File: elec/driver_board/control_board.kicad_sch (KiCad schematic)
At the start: 11 parts, among them J47 button_shutdown, J48 button_mode, J49 rotary_encoder, J50 DCF77 board, J51 RTC, U1 ESP32-C3-DEVKITM-1

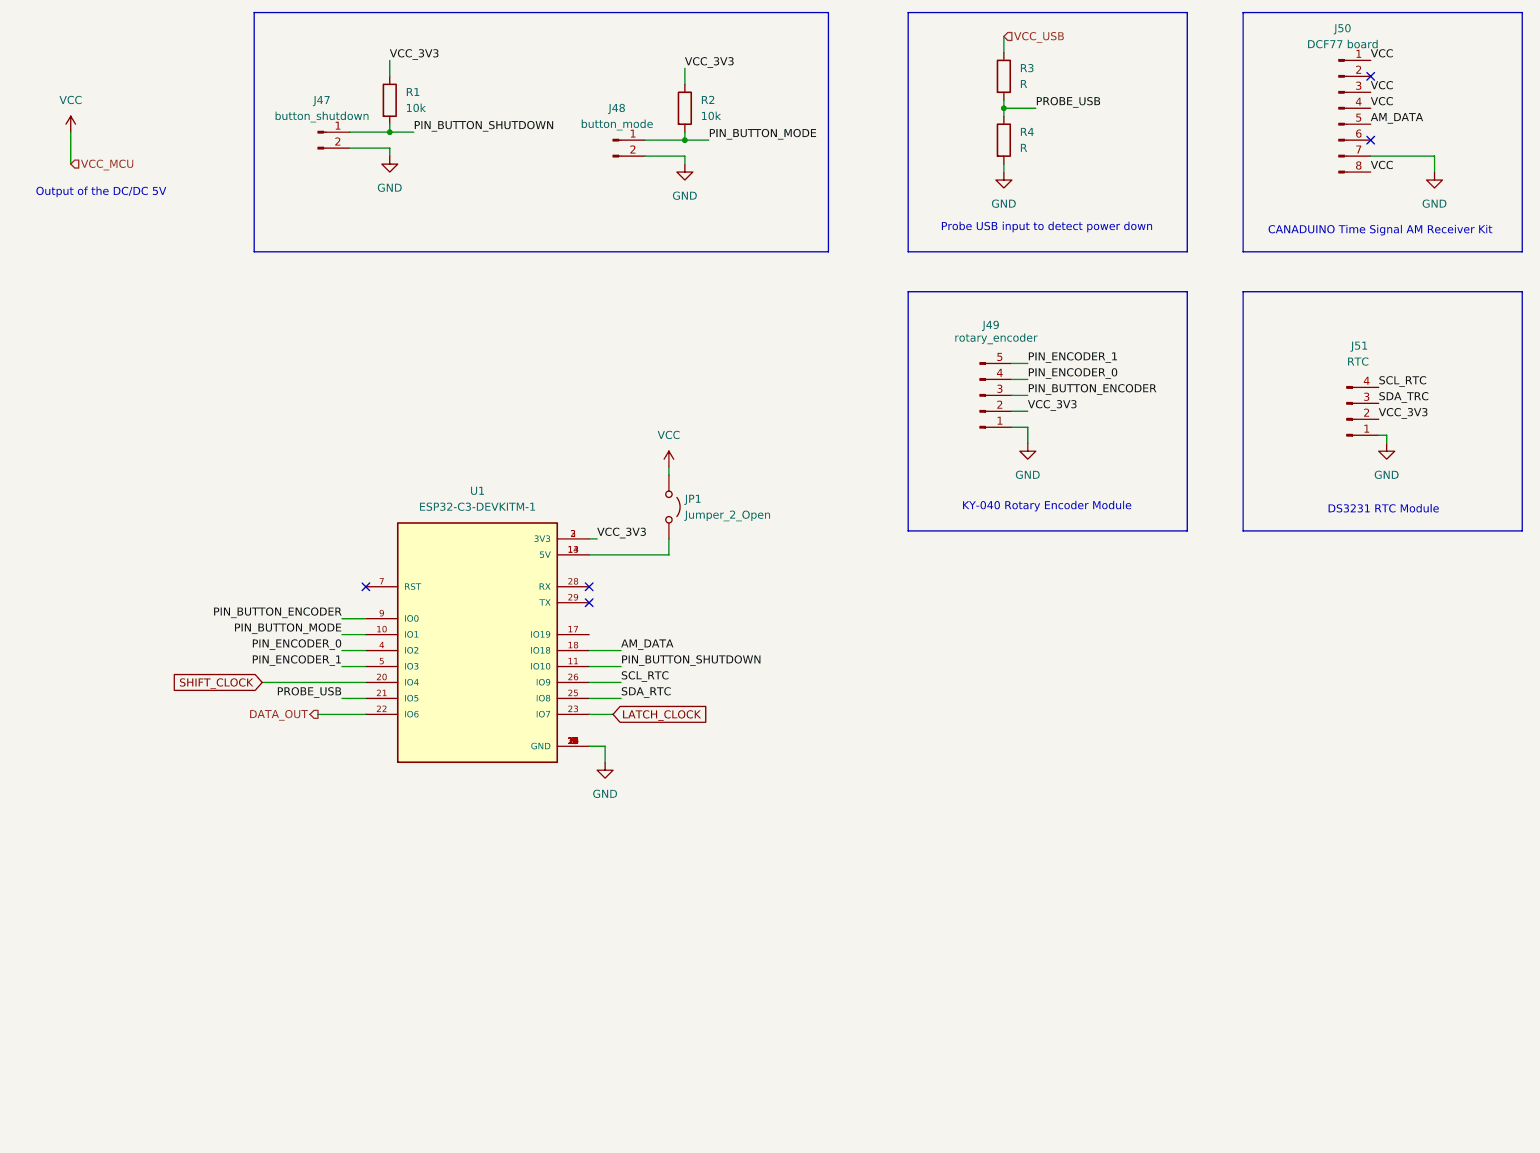
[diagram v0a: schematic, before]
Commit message: [elec] New design with BKA30D-R5
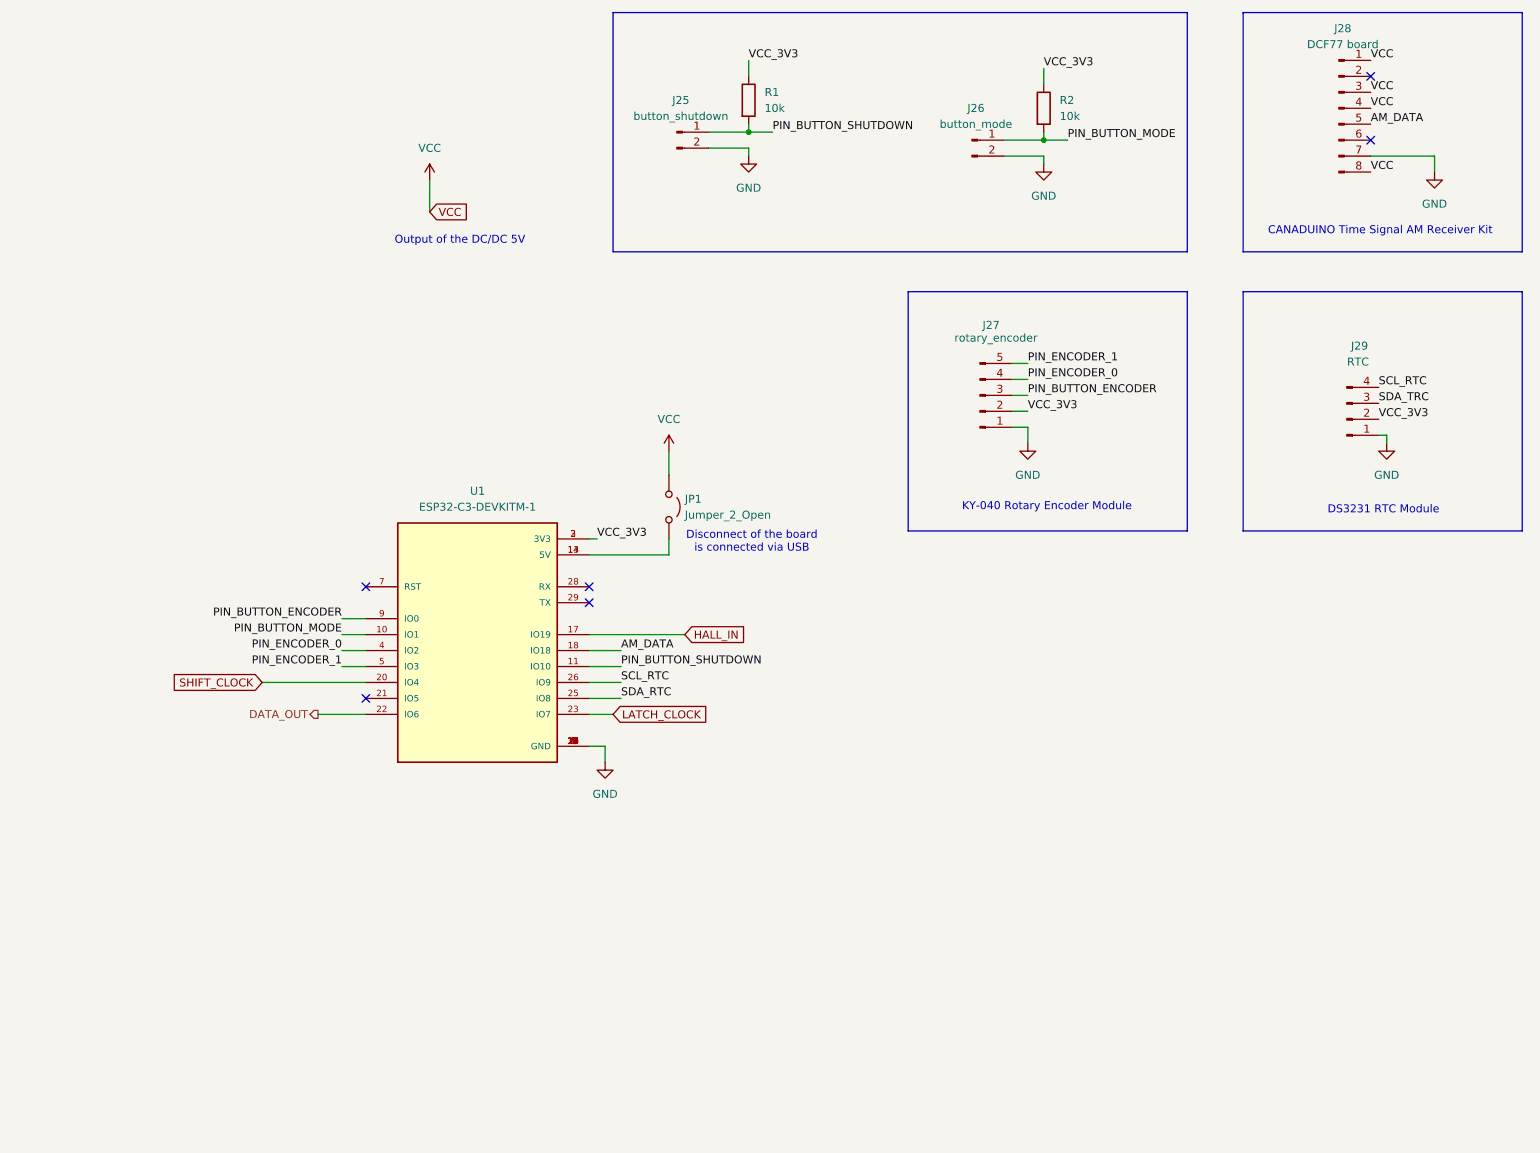
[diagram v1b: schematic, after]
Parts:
- removed R3, R4: R, Resistor_SMD:R_0805_2012Metric, symbol Device:R
- renumbered J47 to J25, J48 to J26, J49 to J27, J50 to J28, J51 to J29
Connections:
- net HALL_IN: now reaches U1.17 (IO19)
- net PROBE_USB: no longer names the net of U1.21 (IO5)
- no-connect marks 5 -> 6
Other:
- note added: "Disconnect of the board is connected via USB"
- note removed: "Probe USB input to detect power down"
- moved on the sheet: J25, J26, R1, R2

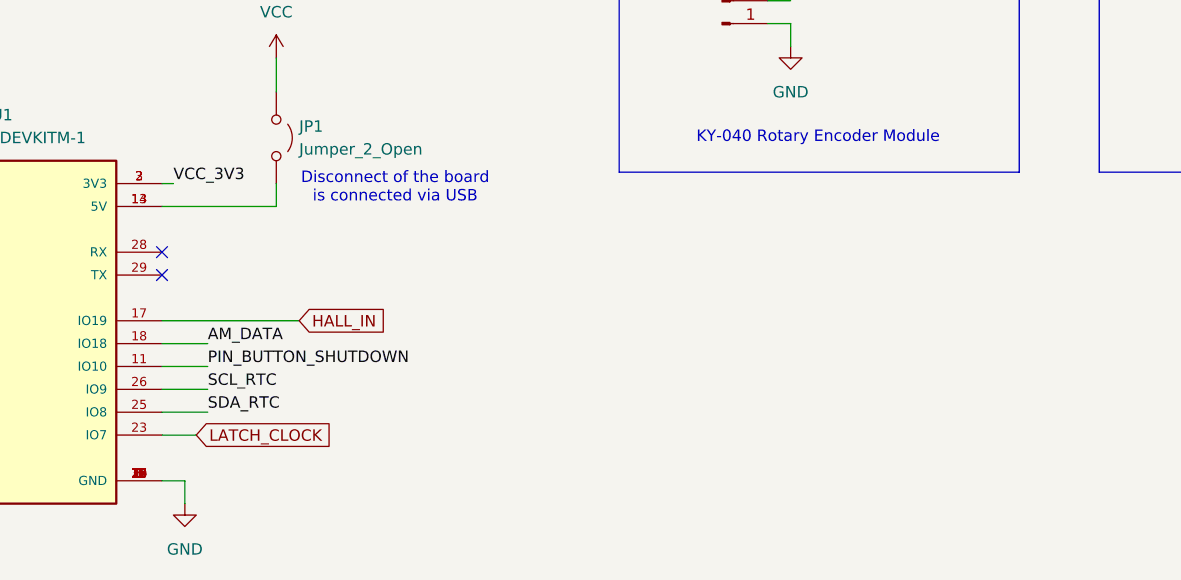
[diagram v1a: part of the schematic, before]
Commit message: [elec] continue routing
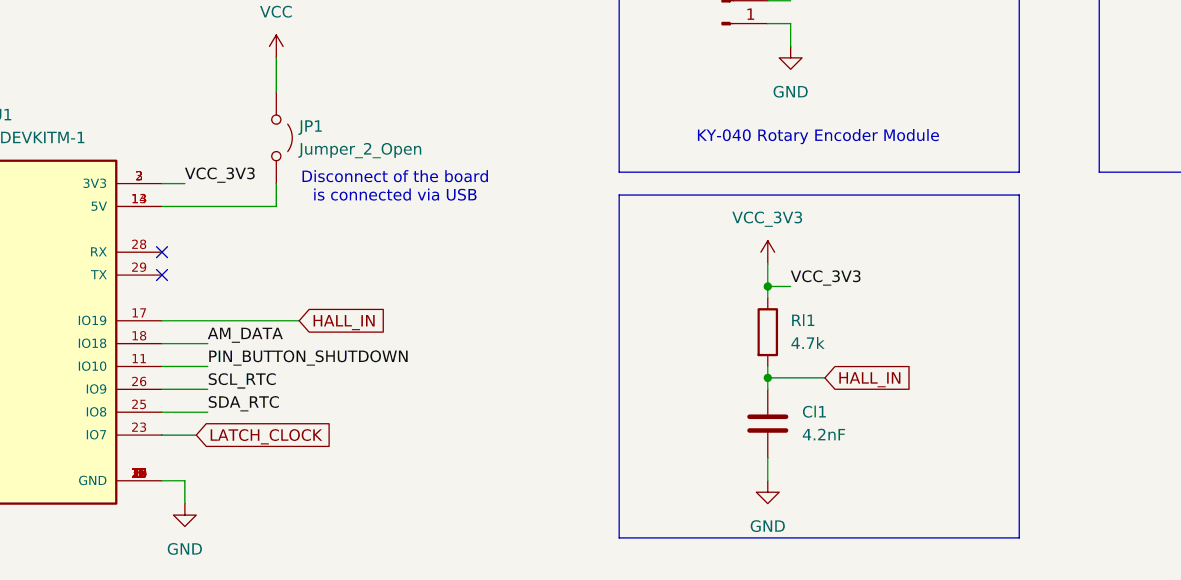
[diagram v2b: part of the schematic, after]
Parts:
- added Cl1: 4.2nF, Capacitor_SMD:C_1206_3216Metric, symbol Device:C
- added Rl1: 4.7k, Capacitor_SMD:C_1206_3216Metric, symbol Device:R
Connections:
- net GND: now also Cl1.2
- net HALL_IN: now also Cl1.1, Rl1.2
- net VCC_3V3: now also Rl1.1

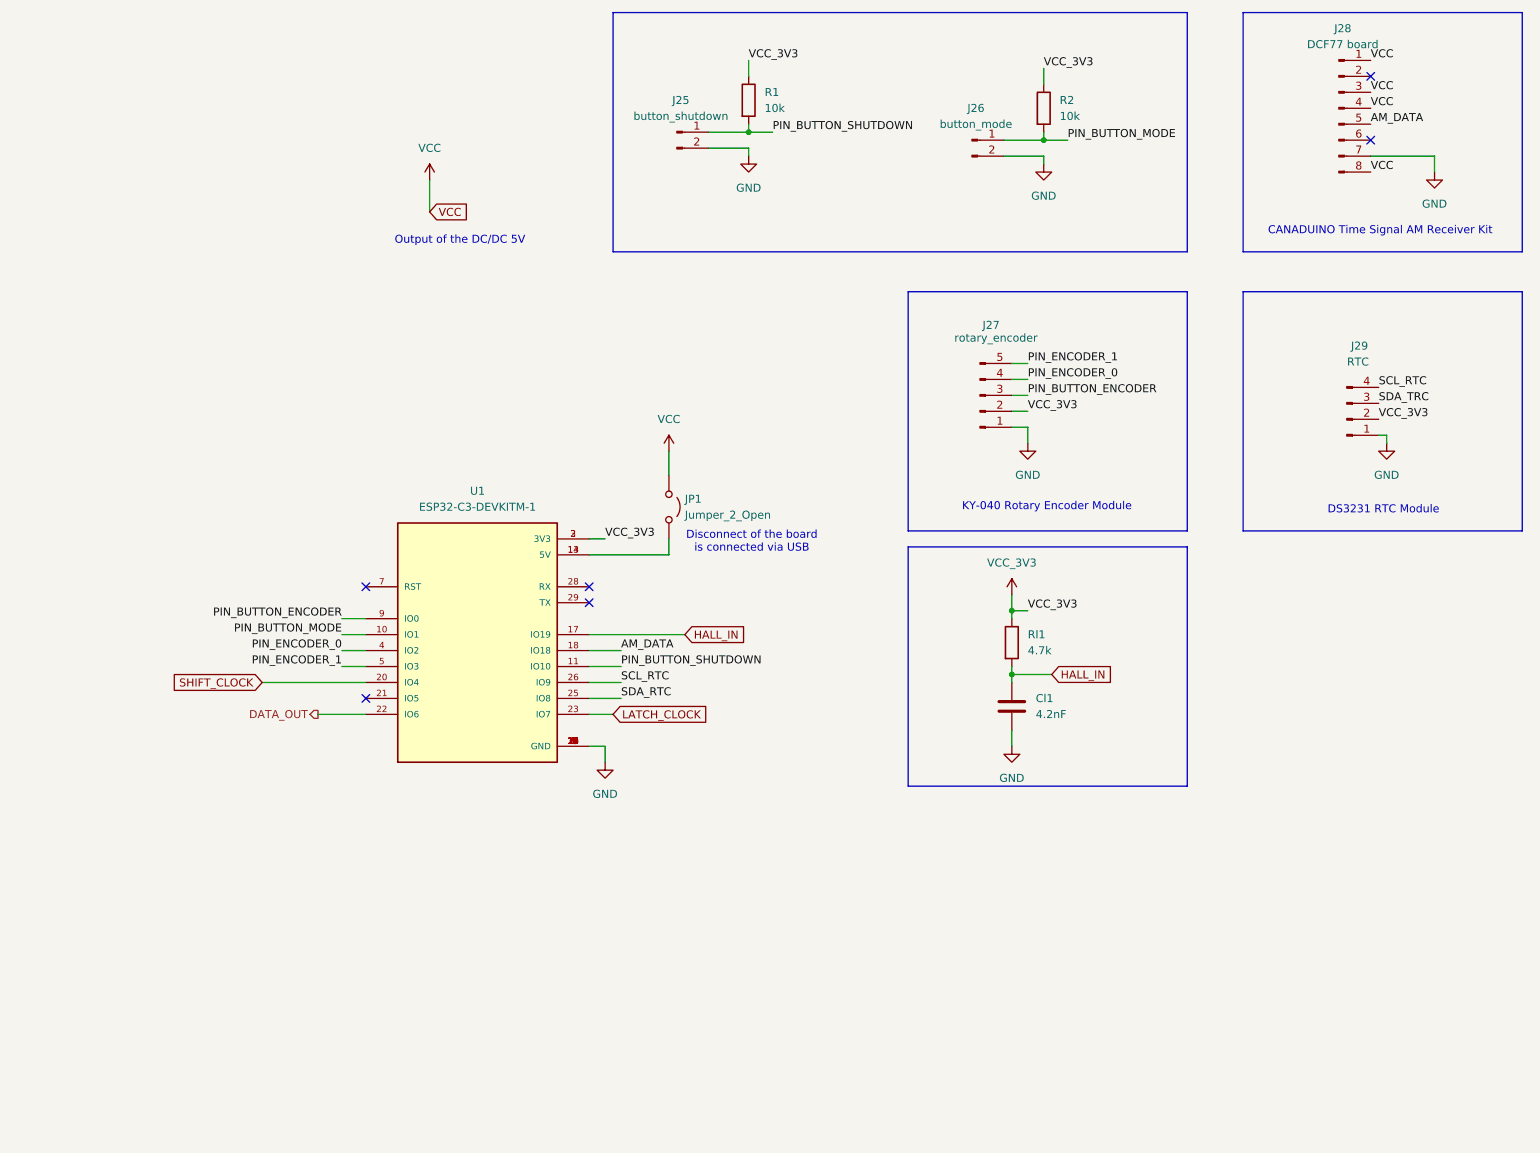
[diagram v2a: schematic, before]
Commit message: [elec] First version of the routing of driver board
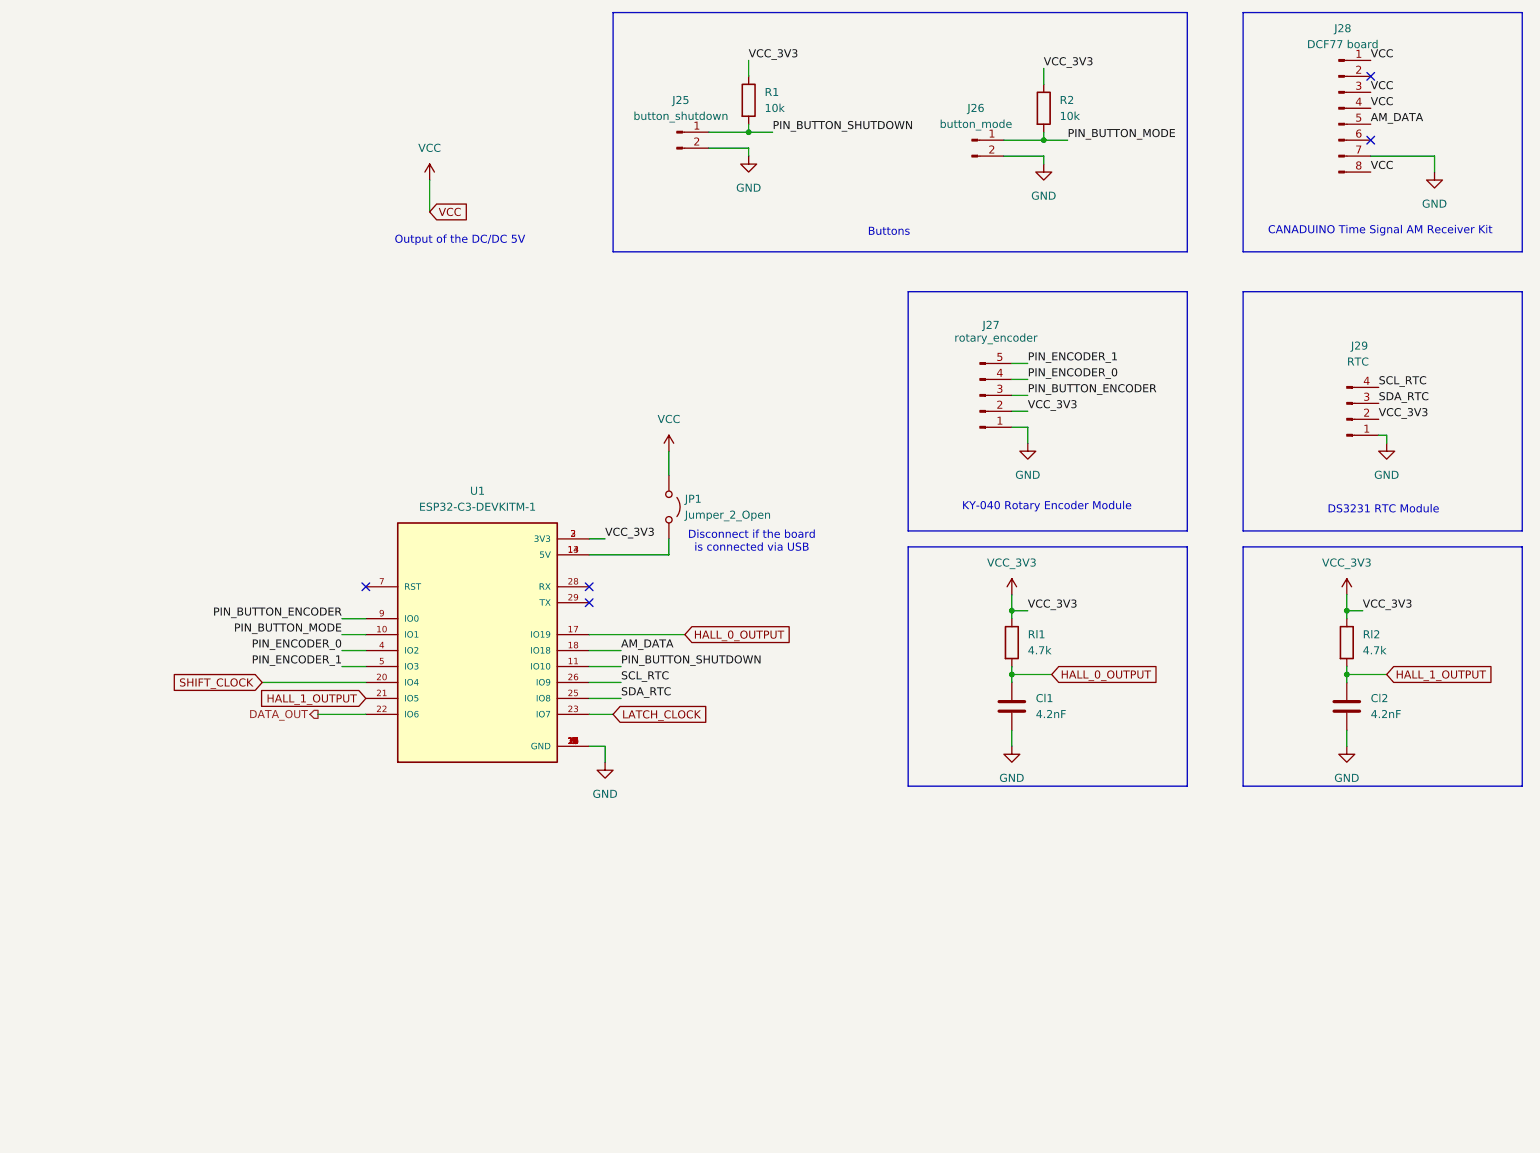
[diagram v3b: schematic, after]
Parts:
- added Cl2: 4.2nF, Capacitor_SMD:C_1206_3216Metric, symbol Device:C
- added Rl2: 4.7k, Capacitor_SMD:C_1206_3216Metric, symbol Device:R
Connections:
- net SDA_TRC is gone; now on net SDA_RTC: J29.3 (Pin_3)
- net GND: now also Cl2.2
- net VCC_3V3: now also Rl2.1
- net HALL_1_OUTPUT: now reaches U1.21 (IO5)
- net HALL_1_OUTPUT: now also Cl2.1, Rl2.2
- net HALL_IN renamed HALL_0_OUTPUT
- no-connect marks 6 -> 5
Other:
- note added: "Buttons"
- note added: "Disconnect if the board is connected via USB"
- note removed: "Disconnect of the board is connected via USB"
